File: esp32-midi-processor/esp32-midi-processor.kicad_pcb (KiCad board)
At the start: 2 copper layers, 108 x 100 mm, 50 parts, among them J1 Midi IN 1, J10 USB Shield right, J11 Spare, J12 Display, J2 Midi IN 2, J3 Midi OUT 1, J4 Midi OUT 2, J5 ESP32 right, J6 ESP32 left, J7 Input Voltage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

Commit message: fix orientation of pinheaders
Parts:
- J10: value USB Shield right -> USB Shield left
- J8: value USB Shield outer left -> USB Shield outer right
- J9: value USB Shield inner left -> USB Shield inner right
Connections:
- net D12 renamed ROTARY_C
- net D14 renamed ROTARY_B
- net D15 renamed USB_RST
- net D18 renamed SCK
- net D19 renamed MISO
- net D21 renamed SDA
- net D22 renamed SCL
- net D23 renamed MOSI
- net D25 renamed SW4
- net D26 renamed ROTARY_SW
- net D27 renamed ROTARY_A
- net D32 renamed SW2
- net D33 renamed SW3
- net D34 renamed Net-(J6-Pin_4)
- net D35 renamed SW1
- net D5 renamed SS
- J6 pad 1: EN -> unconnected-(J6-Pin_1-Pad1)
- J6 pad 2: VP -> unconnected-(J6-Pin_2-Pad2)
- J6 pad 3: VN -> unconnected-(J6-Pin_3-Pad3)
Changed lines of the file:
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@@
 	(net 20 "Net-(J4-PadT)")
 	(net 21 "D2")
-	(net 22 "D19")
+	(net 22 "MISO")
 	(net 23 "D4")
 	(net 24 "RX0")
 	(net 25 "+3V3")
-	(net 26 "D22")
-	(net 27 "D5")
-	(net 28 "D15")
+	(net 26 "SCL")
+	(net 27 "SS")
+	(net 28 "USB_RST")
 	(net 29 "TX0")
-	(net 30 "D23")
+	(net 30 "MOSI")
 	(net 31 "D16")
-	(net 32 "D21")
-	(net 33 "D18")
+	(net 32 "SDA")
+	(net 33 "SCK")
 	(net 34 "D17")
-	(net 35 "VN")
-	(net 36 "D14")
-	(net 37 "D27")
-	(net 38 "D12")
-	(net 39 "D25")
-	(net 40 "D32")
-	(net 41 "D34")
-	(net 42 "D33")
+	(net 35 "unconnected-(J6-Pin_3-Pad3)")
+	(net 36 "ROTARY_B")
+	(net 37 "ROTARY_A")
+	(net 38 "ROTARY_C")
+	(net 39 "SW4")
+	(net 40 "SW2")
+	(net 41 "Net-(J6-Pin_4)")
+	(net 42 "SW3")
 	(net 43 "VIN")
-	(net 44 "EN")
-	(net 45 "D35")
-	(net 46 "VP")
-	(net 47 "D26")
+	(net 44 "unconnected-(J6-Pin_1-Pad1)")
+	(net 45 "SW1")
+	(net 46 "unconnected-(J6-Pin_2-Pad2)")
+	(net 47 "ROTARY_SW")
 	(net 48 "D13")
 	(net 49 "unconnected-(J8-Pin_5-Pad5)")
@@
 			(layers "*.Cu" "*.Mask")
 			(remove_unused_layers no)
-			(net 37 "D27")
+			(net 37 "ROTARY_A")
 			(pinfunction "A")
 			(pintype "passive")
@@
 			(layers "*.Cu" "*.Mask")
 			(remove_unused_layers no)
-			(net 36 "D14")
+			(net 36 "ROTARY_B")
 			(pinfunction "B")
 			(pintype "passive")
@@
 			(layers "*.Cu" "*.Mask")
 			(remove_unused_layers no)
-			(net 38 "D12")
+			(net 38 "ROTARY_C")
 			(pinfunction "C")
 			(pintype "passive")
@@
 			(layers "*.Cu" "*.Mask")
 			(remove_unused_layers no)
-			(net 47 "D26")
+			(net 47 "ROTARY_SW")
 			(pinfunction "S2")
 			(pintype "passive")
@@
 			(layers "F.Cu" "F.Paste" "F.Mask")
 			(roundrect_rratio 0.25)
-			(net 41 "D34")
+			(net 41 "Net-(J6-Pin_4)")
 			(pintype "passive")
 		)
@@
 			(layers "*.Cu" "*.Mask")
 			(remove_unused_layers no)
-			(net 44 "EN")
+			(net 44 "unconnected-(J6-Pin_1-Pad1)")
 			(pinfunction "Pin_1")
-			(pintype "passive")
+			(pintype "passive+no_connect")
 		)
 		(pad "2" thru_hole oval
@@
 			(layers "*.Cu" "*.Mask")
 			(remove_unused_layers no)
-			(net 46 "VP")
+			(net 46 "unconnected-(J6-Pin_2-Pad2)")
 			(pinfunction "Pin_2")
-			(pintype "passive")
+			(pintype "passive+no_connect")
 		)
 		(pad "3" thru_hole oval
@@
 			(layers "*.Cu" "*.Mask")
 			(remove_unused_layers no)
-			(net 35 "VN")
+			(net 35 "unconnected-(J6-Pin_3-Pad3)")
 			(pinfunction "Pin_3")
-			(pintype "passive")
+			(pintype "passive+no_connect")
 		)
 		(pad "4" thru_hole oval
@@
 			(layers "*.Cu" "*.Mask")
 			(remove_unused_layers no)
-			(net 41 "D34")
+			(net 41 "Net-(J6-Pin_4)")
 			(pinfunction "Pin_4")
 			(pintype "passive")
@@
 			(layers "*.Cu" "*.Mask")
 			(remove_unused_layers no)
-			(net 45 "D35")
+			(net 45 "SW1")
 			(pinfunction "Pin_5")
 			(pintype "passive")
@@
 			(layers "*.Cu" "*.Mask")
 			(remove_unused_layers no)
-			(net 40 "D32")
+			(net 40 "SW2")
 			(pinfunction "Pin_6")
 			(pintype "passive")
@@
 			(layers "*.Cu" "*.Mask")
 			(remove_unused_layers no)
-			(net 42 "D33")
+			(net 42 "SW3")
 			(pinfunction "Pin_7")
 			(pintype "passive")
@@
 			(layers "*.Cu" "*.Mask")
 			(remove_unused_layers no)
-			(net 39 "D25")
+			(net 39 "SW4")
 			(pinfunction "Pin_8")
 			(pintype "passive")
@@
 			(layers "*.Cu" "*.Mask")
 			(remove_unused_layers no)
-			(net 47 "D26")
+			(net 47 "ROTARY_SW")
 			(pinfunction "Pin_9")
 			(pintype "passive")
@@
 			(layers "*.Cu" "*.Mask")
 			(remove_unused_layers no)
-			(net 37 "D27")
+			(net 37 "ROTARY_A")
 			(pinfunction "Pin_10")
 			(pintype "passive")
@@
 			(layers "*.Cu" "*.Mask")
 			(remove_unused_layers no)
-			(net 36 "D14")
+			(net 36 "ROTARY_B")
 			(pinfunction "Pin_11")
 			(pintype "passive")
@@
 			(layers "*.Cu" "*.Mask")
 			(remove_unused_layers no)
-			(net 38 "D12")
+			(net 38 "ROTARY_C")
 			(pinfunction "Pin_12")
 			(pintype "passive")
@@
 			(layers "F.Cu" "F.Paste" "F.Mask")
 			(roundrect_rratio 0.25)
-			(net 39 "D25")
+			(net 39 "SW4")
 			(pintype "passive")
 		)
@@
 		(tags "Through hole pin header THT 1x12 2.54mm single row")
 		(property "Reference" "J10"
-			(at 0 -2.33 360)
+			(at 0 -2.33 0)
 			(layer "F.SilkS")
 			(effects
@@
 			)
 		)
-		(property "Value" "USB Shield right"
+		(property "Value" "USB Shield left"
 			(at 2.794 4.826 90)
 			(layer "F.Fab")
@@
 			(layers "*.Cu" "*.Mask")
 			(remove_unused_layers no)
-			(net 27 "D5")
+			(net 27 "SS")
 			(pinfunction "Pin_1")
 			(pintype "passive")
@@
 			(layers "*.Cu" "*.Mask")
 			(remove_unused_layers no)
-			(net 30 "D23")
+			(net 30 "MOSI")
 			(pinfunction "Pin_2")
 			(pintype "passive")
@@
 			(layers "*.Cu" "*.Mask")
 			(remove_unused_layers no)
-			(net 22 "D19")
+			(net 22 "MISO")
 			(pinfunction "Pin_3")
 			(pintype "passive")
@@
 			(layers "*.Cu" "*.Mask")
 			(remove_unused_layers no)
-			(net 33 "D18")
+			(net 33 "SCK")
 			(pinfunction "Pin_4")
 			(pintype "passive")
@@
 			(layers "F.Cu" "F.Paste" "F.Mask")
 			(roundrect_rratio 0.25)
-			(net 47 "D26")
+			(net 47 "ROTARY_SW")
 			(pintype "passive")
 		)
@@
 			(layers "*.Cu" "*.Mask")
 			(remove_unused_layers no)
-			(net 40 "D32")
+			(net 40 "SW2")
 			(pinfunction "2")
 			(pintype "passive")
@@
 			(layers "*.Cu" "*.Mask")
 			(remove_unused_layers no)
-			(net 40 "D32")
+			(net 40 "SW2")
 			(pinfunction "2")
 			(pintype "passive")
@@
 			(layers "F.Cu" "F.Paste" "F.Mask")
 			(roundrect_rratio 0.25)
-			(net 42 "D33")
+			(net 42 "SW3")
 			(pintype "passive")
 		)
@@
 			(layers "*.Cu" "*.Mask")
 			(remove_unused_layers no)
-			(net 45 "D35")
+			(net 45 "SW1")
 			(pinfunction "2")
 			(pintype "passive")
@@
 			(layers "*.Cu" "*.Mask")
 			(remove_unused_layers no)
-			(net 45 "D35")
+			(net 45 "SW1")
 			(pinfunction "2")
 			(pintype "passive")
@@
 		(tags "Through hole pin header THT 1x05 2.54mm single row")
 		(property "Reference" "J9"
-			(at 0 -2.33 360)
+			(at 0 -2.33 0)
 			(layer "F.SilkS")
 			(effects
@@
 			)
 		)
-		(property "Value" "USB Shield inner left"
+		(property "Value" "USB Shield inner right"
 			(at -2.286 7.112 90)
 			(layer "F.Fab")
@@
 			(layers "F.Cu" "F.Paste" "F.Mask")
 			(roundrect_rratio 0.25)
-			(net 45 "D35")
+			(net 45 "SW1")
 			(pintype "passive")
 		)
@@
 			(layers "*.Cu" "*.Mask")
 			(remove_unused_layers no)
-			(net 42 "D33")
+			(net 42 "SW3")
 			(pinfunction "2")
 			(pintype "passive")
@@
 			(layers "*.Cu" "*.Mask")
 			(remove_unused_layers no)
-			(net 42 "D33")
+			(net 42 "SW3")
 			(pinfunction "2")
 			(pintype "passive")
@@
 			(layers "F.Cu" "F.Paste" "F.Mask")
 			(roundrect_rratio 0.25)
-			(net 40 "D32")
+			(net 40 "SW2")
 			(pintype "passive")
 		)
@@
 			(layers "*.Cu" "*.Mask")
 			(remove_unused_layers no)
-			(net 39 "D25")
+			(net 39 "SW4")
 			(pinfunction "2")
 			(pintype "passive")
@@
 			(layers "*.Cu" "*.Mask")
 			(remove_unused_layers no)
-			(net 39 "D25")
+			(net 39 "SW4")
 			(pinfunction "2")
 			(pintype "passive")
@@
 			(layers "*.Cu" "*.Mask")
 			(remove_unused_layers no)
-			(net 26 "D22")
+			(net 26 "SCL")
 			(pinfunction "Pin_3")
 			(pintype "passive")
@@
 			(layers "*.Cu" "*.Mask")
 			(remove_unused_layers no)
-			(net 32 "D21")
+			(net 32 "SDA")
 			(pinfunction "Pin_4")
 			(pintype "passive")
@@
 		(tags "Through hole pin header THT 1x12 2.54mm single row")
 		(property "Reference" "J8"
-			(at 0 -2.33 360)
+			(at 0 -2.33 0)
 			(layer "F.SilkS")
 			(effects
@@
 			)
 		)
-		(property "Value" "USB Shield outer left"
+		(property "Value" "USB Shield outer right"
 			(at 2.286 6.604 90)
 			(layer "F.Fab")
@@
 			(layers "*.Cu" "*.Mask")
 			(remove_unused_layers no)
-			(net 28 "D15")
+			(net 28 "USB_RST")
 			(pinfunction "Pin_10")
 			(pintype "passive")
@@
 			(layers "*.Cu" "*.Mask")
 			(remove_unused_layers no)
-			(net 30 "D23")
+			(net 30 "MOSI")
 			(pinfunction "Pin_1")
 			(pintype "passive")
@@
 			(layers "*.Cu" "*.Mask")
 			(remove_unused_layers no)
-			(net 26 "D22")
+			(net 26 "SCL")
 			(pinfunction "Pin_2")
 			(pintype "passive")
@@
 			(layers "*.Cu" "*.Mask")
 			(remove_unused_layers no)
-			(net 32 "D21")
+			(net 32 "SDA")
 			(pinfunction "Pin_5")
 			(pintype "passive")
@@
 			(layers "*.Cu" "*.Mask")
 			(remove_unused_layers no)
-			(net 22 "D19")
+			(net 22 "MISO")
 			(pinfunction "Pin_6")
 			(pintype "passive")
@@
 			(layers "*.Cu" "*.Mask")
 			(remove_unused_layers no)
-			(net 33 "D18")
+			(net 33 "SCK")
 			(pinfunction "Pin_7")
 			(pintype "passive")
@@
 			(layers "*.Cu" "*.Mask")
 			(remove_unused_layers no)
-			(net 27 "D5")
+			(net 27 "SS")
 			(pinfunction "Pin_8")
 			(pintype "passive")
@@
 			(layers "*.Cu" "*.Mask")
 			(remove_unused_layers no)
-			(net 28 "D15")
+			(net 28 "USB_RST")
 			(pinfunction "Pin_13")
 			(pintype "passive")

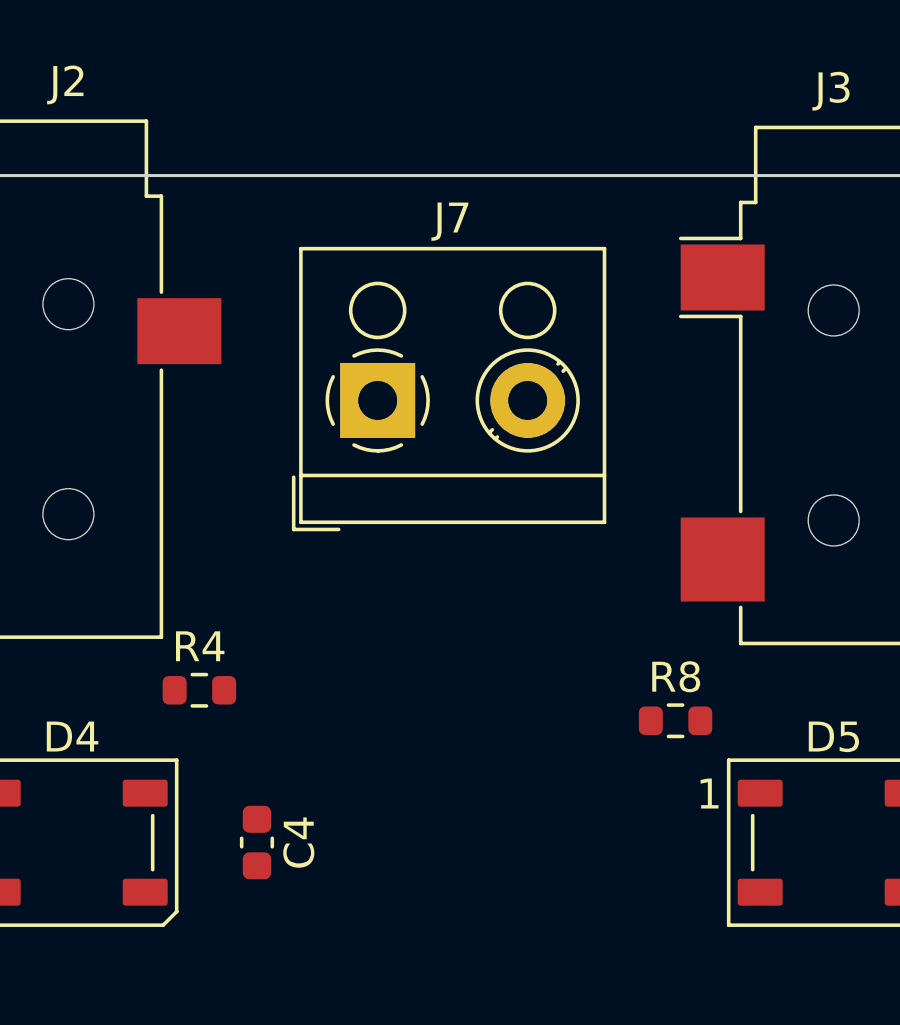
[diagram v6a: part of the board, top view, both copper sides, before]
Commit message: add 7805
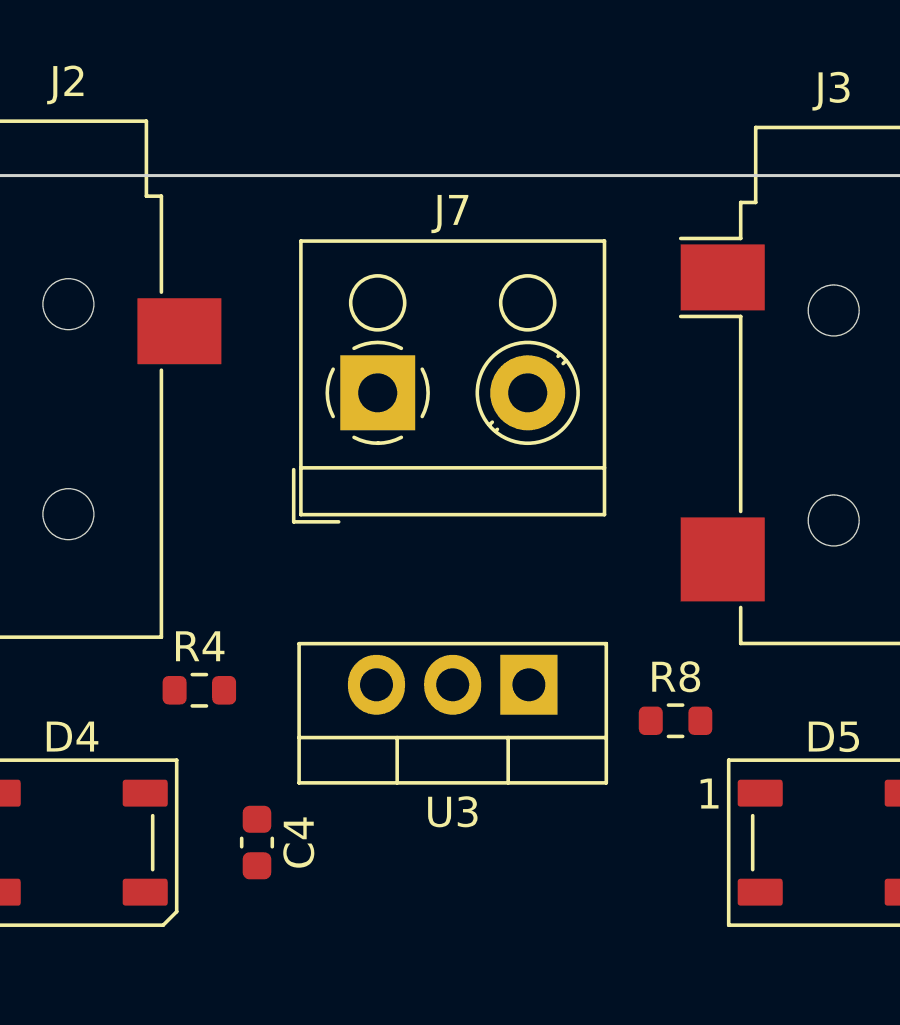
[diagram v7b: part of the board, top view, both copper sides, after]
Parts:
- added U3: LM7805_TO220, Package_TO_SOT_THT:TO-220-3_Vertical, F.Cu at (63.5, 45.5)
- moved J7 0.25 mm to (58.5, 35.8)
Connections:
- J7 pad 2: VIN -> Net-(J7-Pin_2)

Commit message: finish pcb
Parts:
- removed J11: Spare, Connector_PinHeader_2.54mm:PinHeader_1x05_P2.54mm_Vertical
- added J13: Spare, Connector_PinHeader_2.54mm:PinHeader_1x04_P2.54mm_Vertical, F.Cu at (22.2, 101.3)
- U1, U2: footprint Package_DIP:DIP-8_W7.62mm_Socket -> Package_SO:SOP-8_6.605x9.655mm_P2.54mm
- moved D1 9.72 mm to (22.8, 65.8), turned to -90 degrees
- moved D2 7.24 mm to (44.5, 65.5), turned to -90 degrees
- moved U2 5.90 mm to (52.2, 65.2)
- moved U1 3.96 mm to (30.1, 65.7)
- moved C2 3.18 mm to (60.7, 69.2)
- moved R5 3.18 mm to (61.2, 65.0)
- moved R6 3.18 mm to (61.2, 60.9)
- moved C1 2.74 mm to (38.7, 71.2)
- moved R3 2.74 mm to (39.0, 62.6)
- moved R2 2.74 mm to (39.0, 66.9)
- moved J3 0.46 mm to (73.7, 35.1)
- moved J4 0.46 mm to (90.2, 35.1)
- moved J1 0.25 mm to (31.8, 35.1)
- moved J2 0.25 mm to (48.1, 35.1)
- turned JP1 to -90 degrees
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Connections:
- J6 pad 13: D13 -> GPX
- J9 pad 3: unconnected-(J9-Pin_3-Pad3) -> GPX
- U3 pad 3: VIN -> +5V
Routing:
- net +3V3: track 0.00 -> 391.7 mm, vias 0 -> 8
- net GPX: track 0.00 -> 151.8 mm, vias 0 -> 2
- net SW4: track 0.00 -> 138.2 mm
- net SW3: track 0.00 -> 124.7 mm
- net ROTARY_SW: track 0.00 -> 113.7 mm, vias 0 -> 2
- net SW2: track 0.00 -> 111.2 mm
- net USB_RST: track 0.00 -> 104.3 mm
- net ROTARY_B: track 0.00 -> 101.5 mm, vias 0 -> 2
- net ROTARY_C: track 0.00 -> 101.2 mm, vias 0 -> 4
- net SS: track 0.00 -> 99.0 mm, vias 0 -> 2
- net SW1: track 0.00 -> 97.6 mm
- net ROTARY_A: track 0.00 -> 95.1 mm, vias 0 -> 2
- net MISO: track 0.00 -> 83.6 mm, vias 0 -> 2
- net SCK: track 0.00 -> 81.5 mm, vias 0 -> 2
- net MOSI: track 0.00 -> 81.4 mm, vias 0 -> 2
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- added copper zone on F.Cu, net +5V
- added copper zone on B.Cu, net GND
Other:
- board size 108 x 100 mm -> 108 x 97.4 mm
- board text added: "Rev. 20250102"
- board text removed: "Rev xxx"
